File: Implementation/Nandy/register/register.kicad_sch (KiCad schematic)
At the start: 45 parts, among them J3 Conn_01x04_Male

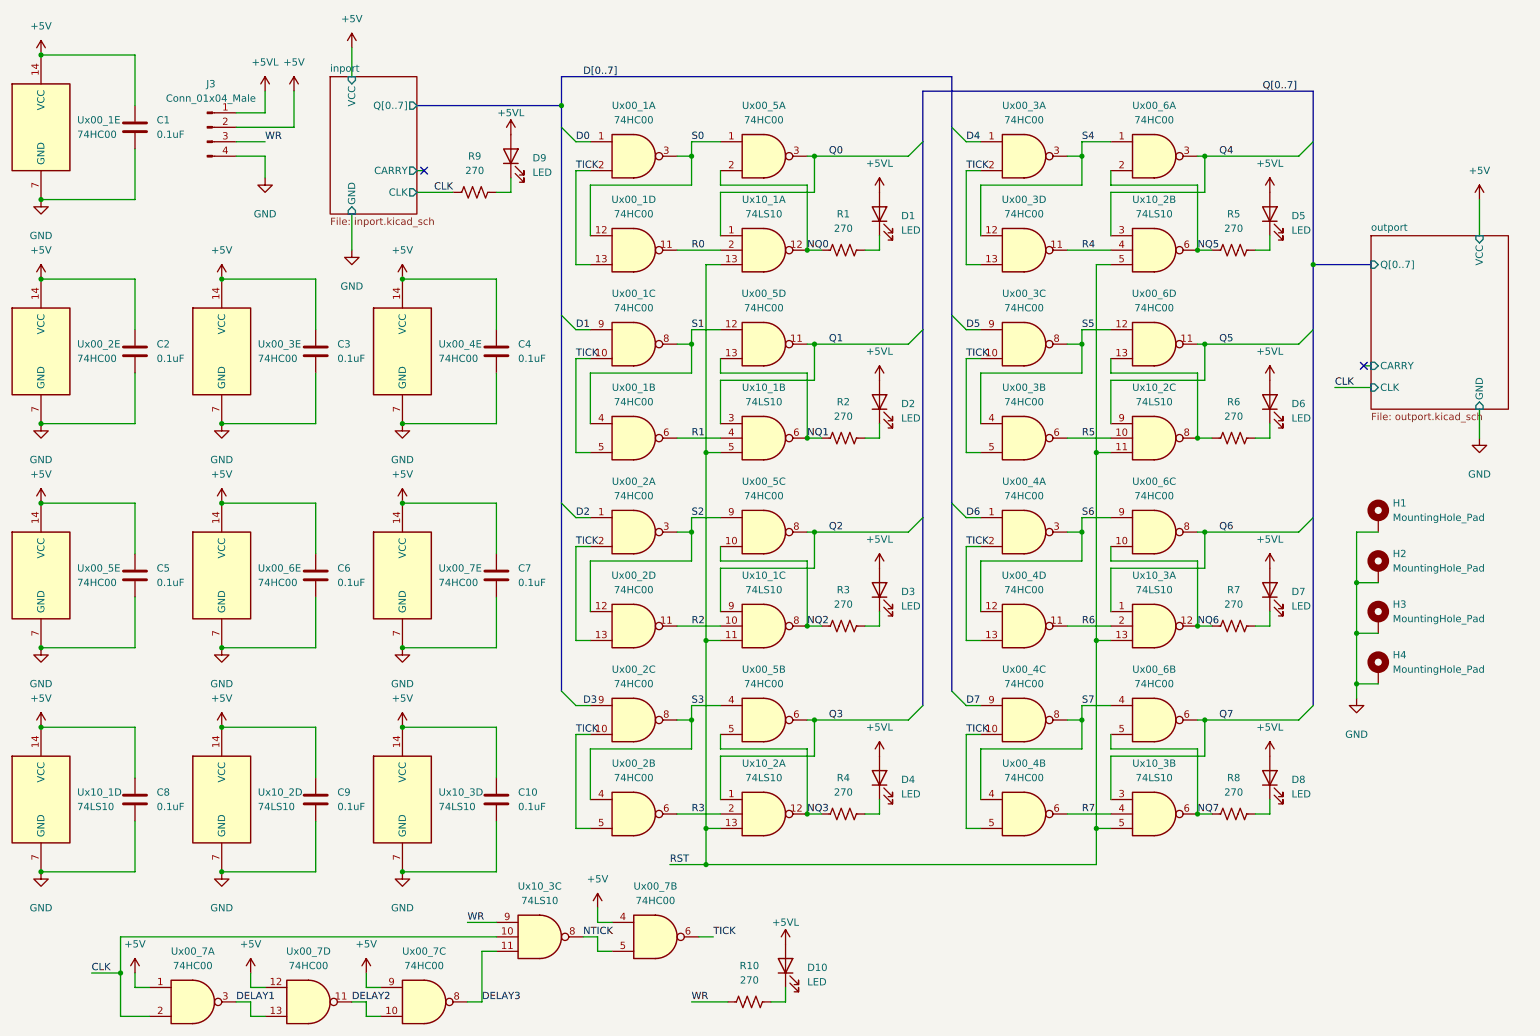
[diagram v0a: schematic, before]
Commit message: Updated register to kicad7
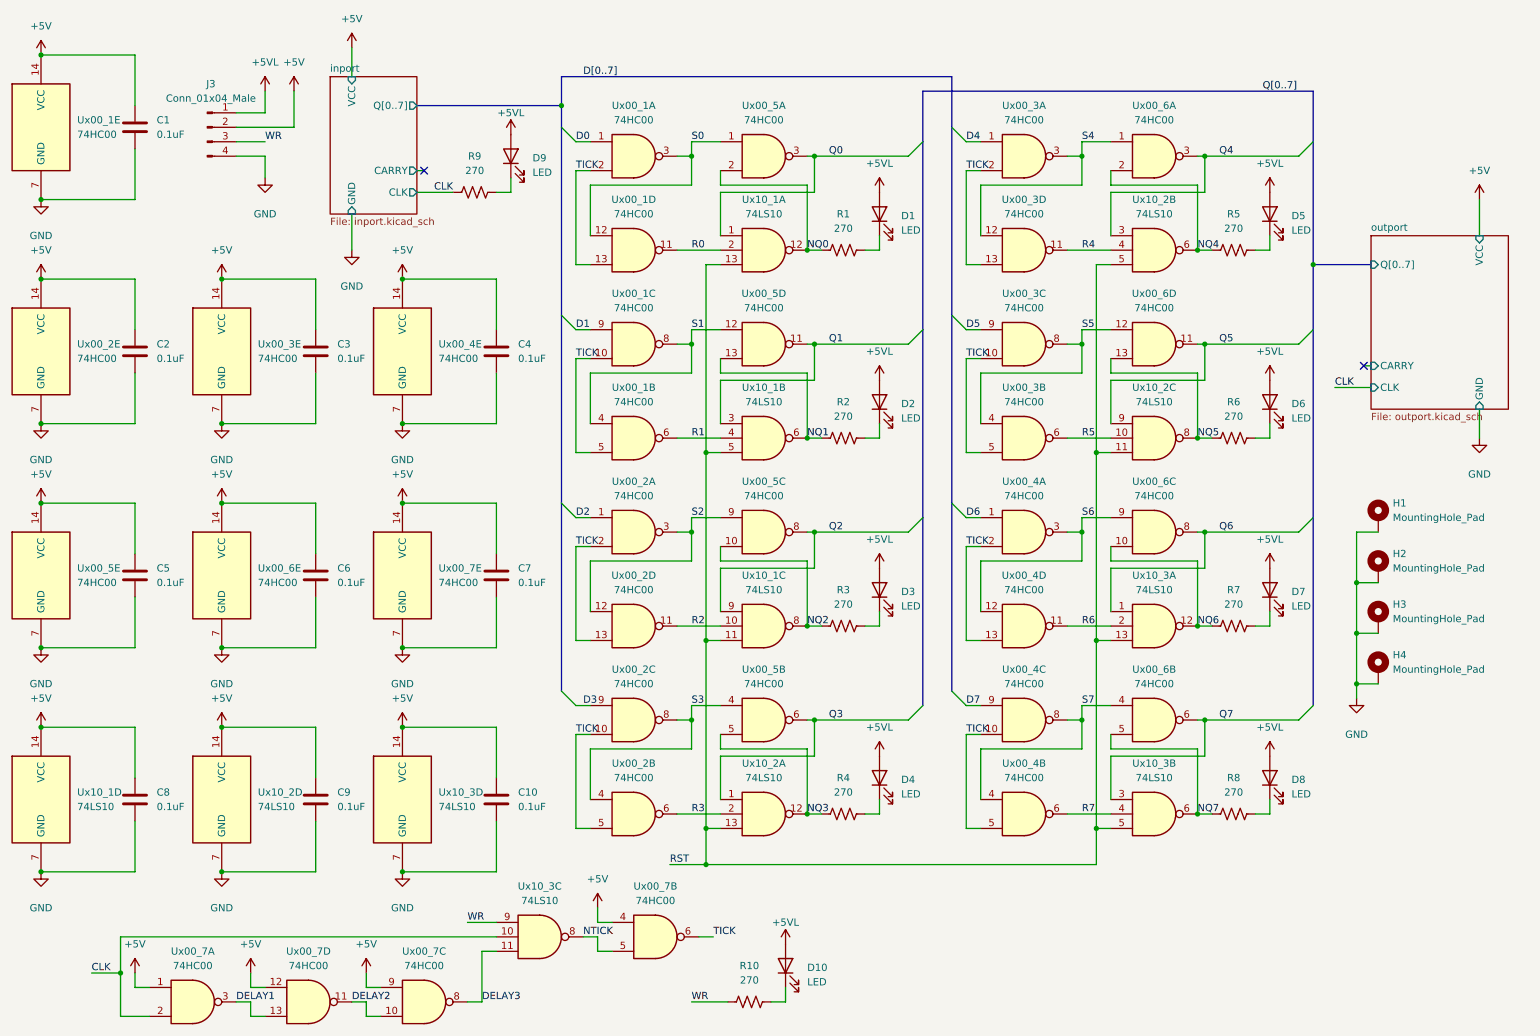
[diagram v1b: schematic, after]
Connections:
- net NQ5: now also R6.1, Ux00_6.13, Ux10_2.8; no longer R5.1, Ux00_6.2, Ux10_2.6
- new net NQ4: R5.1, Ux00_6.2, Ux10_2.6
